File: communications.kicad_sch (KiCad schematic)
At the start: 1 part

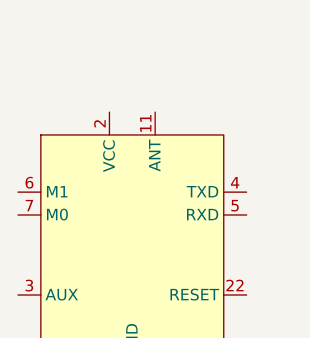
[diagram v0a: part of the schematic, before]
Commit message: Wired barometers and GPS up, added misc LEDs, tidy-up
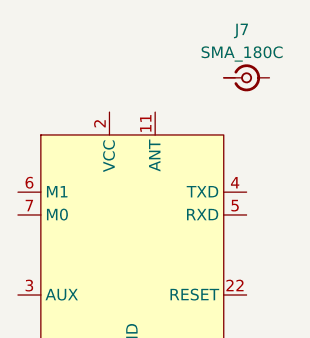
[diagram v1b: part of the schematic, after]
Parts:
- added J7: SMA_180C, Valkyrie_footprints:SMA_180C, symbol Connector:Conn_Coaxial_Small
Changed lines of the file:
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@@
+	)
+	(symbol
+		(lib_id "Connector:Conn_Coaxial_Small")
+		(at 121.92 57.15 0)
+		(unit 1)
+		(exclude_from_sim no)
+		(in_bom yes)
+		(on_board yes)
+		(dnp no)
+		(property "Reference" "J7"
+			(at 121.412 51.816 0)
+			(effects
+				(font
+					(size 1.27 1.27)
+				)
+			)
+		)
+		(property "Value" "SMA_180C"
+			(at 121.412 54.356 0)
+			(effects
+				(font
+					(size 1.27 1.27)
+				)
+			)
+		)
+		(property "Footprint" "Valkyrie_footprints:SMA_180C"
+			(at 121.92 57.15 0)
+			(effects
+				(font
+					(size 1.27 1.27)
+				)
+				(hide yes)
+			)
+		)
+		(property "Datasheet" "https://www.direnc.net/sma-180c-disi-konnektor-dar-ayakli-sa0n1s0g"
+			(at 121.92 57.15 0)
+			(effects
+				(font
+					(size 1.27 1.27)
+				)
+				(hide yes)
+			)
+		)
+		(property "Description" "small coaxial connector (BNC, SMA, SMB, SMC, Cinch/RCA, LEMO, ...)"
+			(at 121.92 57.15 0)
+			(effects
+				(font
+					(size 1.27 1.27)
+				)
+				(hide yes)
+			)
+		)
+		(pin "1"
+		)
+		(pin "2"
+		)
+		(instances
+			(project "valkyriev3"
+				(path "/d24fd15c-a242-4d26-9876-7755ca0d378c/15c0363f-221d-49cb-89b5-29e3b8f192aa"
+					(reference "J7")
+					(unit 1)
+				)
+			)
+		)
 	)
 	(symbol

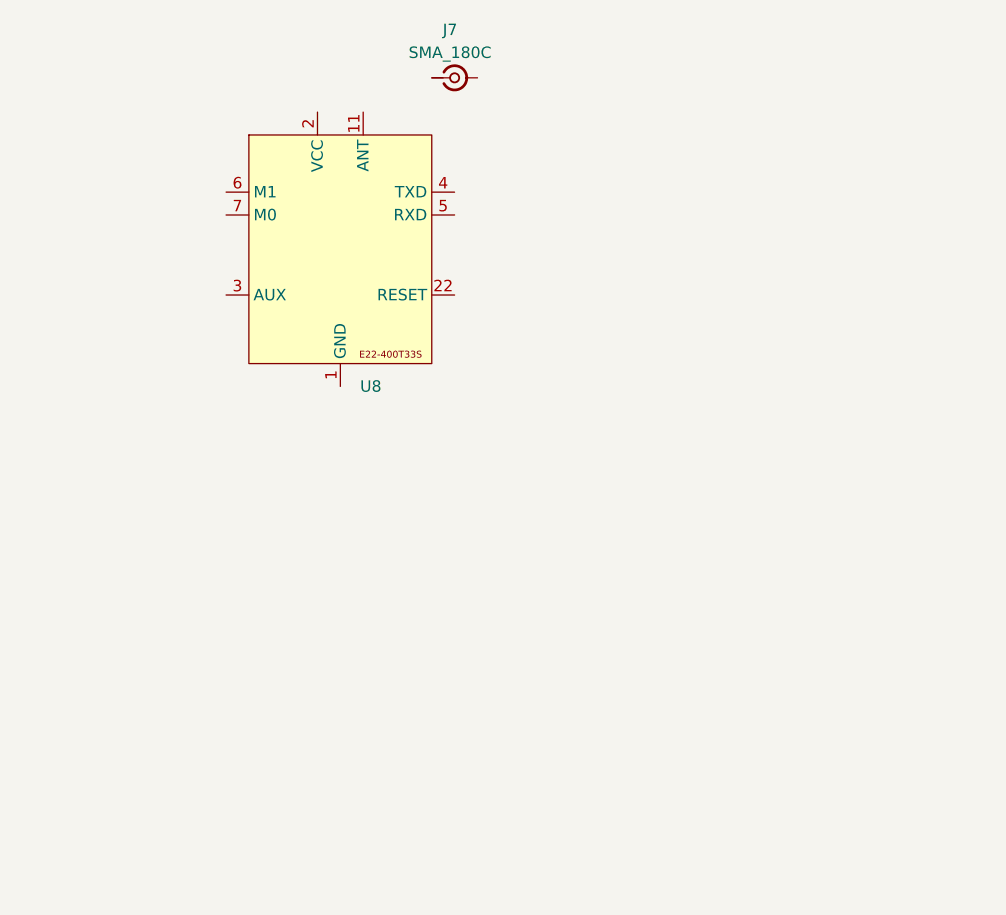
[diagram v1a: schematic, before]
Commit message: preliminary schematic wired, all footprints assigned, all laid out in PCB editor.
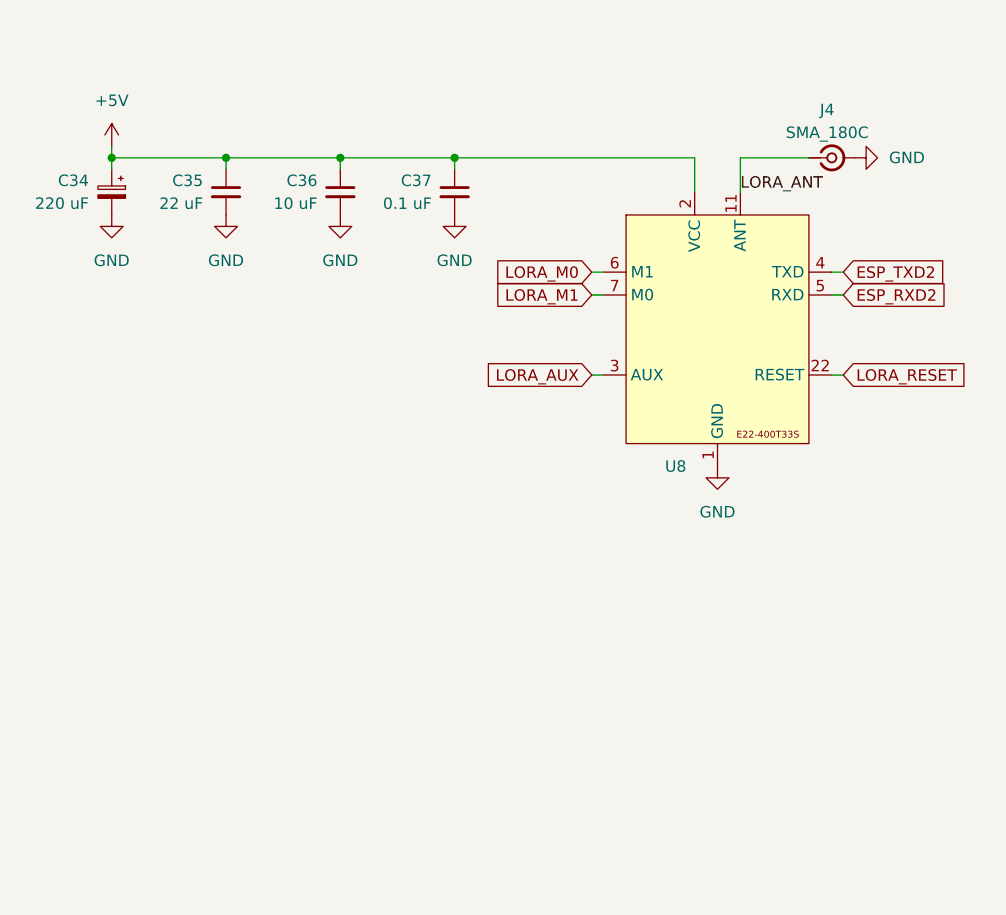
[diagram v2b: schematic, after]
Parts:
- added C34: 220 uF, Capacitor_SMD:CP_Elec_6.3x7.7, symbol Device:C_Polarized_Small
- added C35: 22 uF, Capacitor_SMD:C_0805_2012Metric, symbol Device:C_Small
- added C36: 10 uF, Capacitor_SMD:C_0603_1608Metric, symbol Device:C_Small
- added C37: 0.1 uF, Capacitor_SMD:C_0805_2012Metric, symbol Device:C_Small
- renumbered J7 to J4
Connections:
- net GND: now also J4.2 (Ext), C34.2, C35.2, C36.2, C37.2
- net LORA_ANT: now reaches J4.1 (In)
- net LORA_ANT: now also U8.11 (ANT)
- net +5V: now reaches U8.2 (VCC)
- net +5V: now also C34.1, C35.1, C36.1, C37.1
- net LORA_RESET: now reaches U8.22 (RESET)
- net LORA_AUX: now reaches U8.3 (AUX)
- net ESP_TXD2: now reaches U8.4 (TXD)
- net ESP_RXD2: now reaches U8.5 (RXD)
- net LORA_M0: now reaches U8.6 (M1)
- net LORA_M1: now reaches U8.7 (M0)
- now unconnected: U8.18 (NC), U8.19 (NC), U8.20 (NC), U8.21 (NC), U8.24 (NC)
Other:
- moved on the sheet: J4, U8

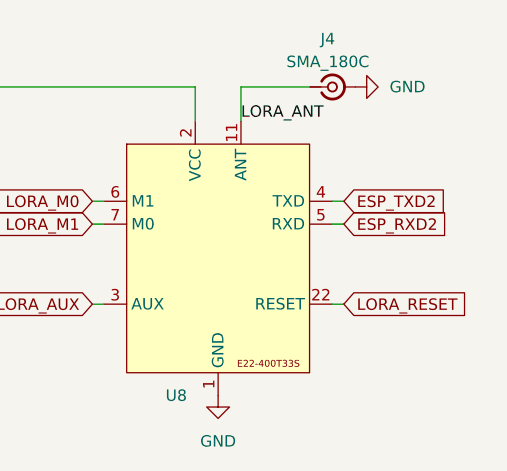
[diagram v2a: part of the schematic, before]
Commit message: reassigned some footprints, preliminary PCB layout
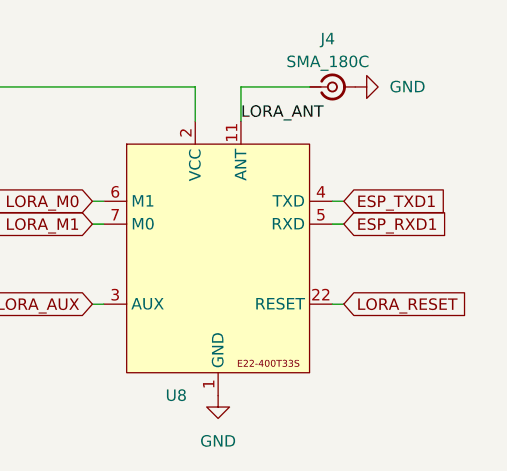
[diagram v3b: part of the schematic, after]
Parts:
- C35, C37: footprint Capacitor_SMD:C_0805_2012Metric -> Capacitor_SMD:C_0603_1608Metric
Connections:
- net ESP_RXD2 renamed ESP_RXD1
- net ESP_TXD2 renamed ESP_TXD1
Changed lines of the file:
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@@
 		)
 	)
-	(global_label "ESP_RXD2"
+	(global_label "ESP_RXD1"
 		(shape input)
 		(at 165.1 81.28 0)
@@
 		)
 	)
-	(global_label "ESP_TXD2"
+	(global_label "ESP_TXD1"
 		(shape input)
 		(at 165.1 78.74 0)
@@
 			)
 		)
-		(property "Footprint" "Capacitor_SMD:C_0805_2012Metric"
+		(property "Footprint" "Capacitor_SMD:C_0603_1608Metric"
 			(at 96.52 69.85 0)
 			(effects
@@
 			)
 		)
-		(property "Footprint" "Capacitor_SMD:C_0805_2012Metric"
+		(property "Footprint" "Capacitor_SMD:C_0603_1608Metric"
 			(at 121.92 69.85 0)
 			(effects

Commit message: updated some values and routed some preliminary roads
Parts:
- J4: footprint Valkyrie_footprints:SMA_180C -> Connector_Coaxial:SMA_Amphenol_132134-16_Vertical
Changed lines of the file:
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@@
 			)
 		)
-		(property "Footprint" "Valkyrie_footprints:SMA_180C"
+		(property "Footprint" "Connector_Coaxial:SMA_Amphenol_132134-16_Vertical"
 			(at 163.83 66.04 0)
 			(effects
@@
 			)
 		)
-		(property "Datasheet" "https://www.direnc.net/sma-180c-disi-konnektor-dar-ayakli-sa0n1s0g"
+		(property "Datasheet" "https://www.direnc.net/sma-180c-disi-konnektor-genis-ayak-aralikli-sa0n1t0g"
 			(at 163.83 66.04 0)
 			(effects

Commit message: did some clean-up, did some to-do tasks.
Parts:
- added Q6, Q7: BC817, Package_TO_SOT_SMD:SOT-23, symbol Transistor_BJT:BC817
- added R24, R25, R26, R27: 1k, Resistor_SMD:R_0603_1608Metric, symbol Device:R_Small
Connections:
- net ESP_RXD1: now also U8.4 (TXD); no longer U8.5 (RXD)
- net ESP_TXD1: now also U8.5 (RXD); no longer U8.4 (TXD)
- net GND: now also Q6.2 (E), Q7.2 (E)
- net LORA_M0: now also R27.2; no longer U8.6 (M1)
- net LORA_M1: now also R25.2; no longer U8.7 (M0)
- new net +3V3: R24.1, R26.1
- new net LORA_M0_B: Q7.1 (B), R27.1
- new net LORA_M0_C: Q7.3 (C), R26.2, U8.7 (M0)
- new net LORA_M1_B: Q6.1 (B), R25.1
- new net LORA_M1_C: Q6.3 (C), R24.2, U8.6 (M1)
